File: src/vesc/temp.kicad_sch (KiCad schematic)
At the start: 3 parts

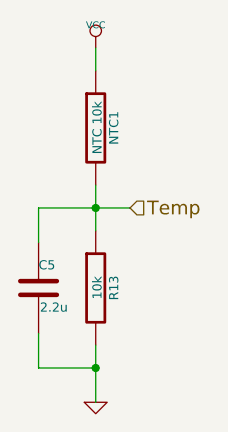
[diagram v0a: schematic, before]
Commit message: Fix component values
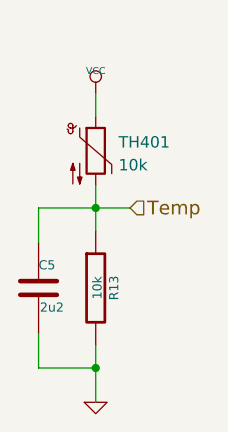
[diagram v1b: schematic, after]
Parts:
- removed NTC1: NTC 10k, Resistor_SMD:R_0603_1608Metric, symbol BLDC_4-rescue:R-RESCUE-BLDC_4
- added TH401: 10k, symbol Device:Thermistor_NTC
- C5: value 2.2u -> 2u2; footprint Capacitor_SMD:C_0603_1608Metric -> (none)
- R13: footprint Resistor_SMD:R_0603_1608Metric -> (none)
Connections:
- net Temp: now also TH401.2
- net VCC: now also TH401.1
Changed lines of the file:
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@@
 	(wire
 		(pts
-			(xy 147.32 74.93) (xy 147.32 77.47)
+			(xy 147.32 80.01) (xy 147.32 82.55)
 		)
 		(stroke
@@
 	(symbol
 		(lib_id "BLDC_4-rescue:R-RESCUE-BLDC_4")
-		(at 147.32 83.82 0)
-		(unit 1)
-		(exclude_from_sim no)
-		(in_bom yes)
-		(on_board yes)
-		(dnp no)
-		(property "Reference" "NTC1"
-			(at 149.352 83.82 90)
-			(effects
-				(font
-					(size 1.016 1.016)
-				)
-			)
-		)
-		(property "Value" "NTC 10k"
-			(at 147.4978 83.7946 90)
-			(effects
-				(font
-					(size 1.016 1.016)
-				)
-			)
-		)
-		(property "Footprint" "Resistor_SMD:R_0603_1608Metric"
-			(at 145.542 83.82 90)
-			(effects
-				(font
-					(size 0.762 0.762)
-				)
-				(hide yes)
-			)
-		)
-		(property "Datasheet" ""
-			(at 147.32 83.82 0)
-			(effects
-				(font
-					(size 0.762 0.762)
-				)
-			)
-		)
-		(property "Description" ""
-			(at 147.32 83.82 0)
-			(effects
-				(font
-					(size 1.27 1.27)
-				)
-			)
-		)
-		(pin "1"
-		)
-		(pin "2"
-		)
-		(instances
-			(project "Cheap FOCer 2 60mm"
-				(path "/8b53313b-c20e-4d2c-aeda-56c30dbca1c0/00000000-0000-0000-0000-000053ffb3e2"
-					(reference "NTC1")
-					(unit 1)
-				)
-			)
-		)
-	)
-	(symbol
-		(lib_id "BLDC_4-rescue:R-RESCUE-BLDC_4")
 		(at 147.32 101.6 0)
 		(unit 1)
@@
 			)
 		)
-		(property "Footprint" "Resistor_SMD:R_0603_1608Metric"
+		(property "Footprint" ""
 			(at 145.542 101.6 90)
 			(effects
@@
 			)
 		)
-		(property "Value" "2.2u"
+		(property "Value" "2u2"
 			(at 141.1224 103.759 0)
 			(effects
@@
 			)
 		)
-		(property "Footprint" "Capacitor_SMD:C_0603_1608Metric"
+		(property "Footprint" ""
 			(at 141.9352 105.41 0)
 			(effects
@@
 	(symbol
 		(lib_id "BLDC_4-rescue:VCC")
-		(at 147.32 74.93 0)
+		(at 147.32 80.01 0)
 		(unit 1)
 		(exclude_from_sim no)
@@
 		(dnp no)
 		(property "Reference" "#PWR021"
-			(at 147.32 72.39 0)
+			(at 147.32 77.47 0)
 			(effects
 				(font
@@
 		)
 		(property "Value" "VCC"
-			(at 147.32 72.39 0)
-			(effects
-				(font
-					(size 0.762 0.762)
-				)
-			)
-		)
-		(property "Footprint" ""
-			(at 147.32 74.93 0)
+			(at 147.32 77.47 0)
+			(effects
+				(font
+					(size 0.762 0.762)
+				)
+			)
+		)
+		(property "Footprint" ""
+			(at 147.32 80.01 0)
 			(effects
 				(font
@@
 		)
 		(property "Datasheet" ""
-			(at 147.32 74.93 0)
+			(at 147.32 80.01 0)
 			(effects
 				(font
@@
 		)
 		(property "Description" ""
-			(at 147.32 74.93 0)
+			(at 147.32 80.01 0)
 			(effects
 				(font
@@
 					(unit 1)
 				)
+			)
+		)
+	)
+	(symbol
+		(lib_id "Device:Thermistor_NTC")
+		(at 147.32 86.36 0)
+		(unit 1)
+		(exclude_from_sim no)
+		(in_bom yes)
+		(on_board yes)
+		(dnp no)
+		(fields_autoplaced yes)
+		(property "Reference" "TH401"
+			(at 149.86 85.4074 0)
+			(effects
+				(font
+					(size 1.27 1.27)
+				)
+				(justify left)
+			)
+		)
+		(property "Value" "10k"
+			(at 149.86 87.9474 0)
+			(effects
+				(font
+					(size 1.27 1.27)
+				)
+				(justify left)
+			)
+		)
+		(property "Footprint" ""
+			(at 147.32 85.09 0)
+			(effects
+				(font
+					(size 1.27 1.27)
+				)
+				(hide yes)
+			)
+		)
+		(property "Datasheet" "~"
+			(at 147.32 85.09 0)
+			(effects
+				(font
+					(size 1.27 1.27)
+				)
+				(hide yes)
+			)
+		)
+		(property "Description" "Temperature dependent resistor, negative temperature coefficient"
+			(at 147.32 86.36 0)
+			(effects
+				(font
+					(size 1.27 1.27)
+				)
+				(hide yes)
+			)
+		)
+		(pin "2"
+		)
+		(pin "1"
+		)
+		(instances
+			(project ""
+				(path "/8b53313b-c20e-4d2c-aeda-56c30dbca1c0/00000000-0000-0000-0000-000053ffb3e2"
+					(reference "TH401")
+					(unit 1)
+				)

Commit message: footprints - most resistors and caps, some ICs
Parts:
- C5: footprint (none) -> Capacitor_SMD:C_0201_0603Metric
- R13, TH401: footprint (none) -> Resistor_SMD:R_0402_1005Metric
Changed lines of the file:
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@@
 			)
 		)
-		(property "Footprint" ""
+		(property "Footprint" "Resistor_SMD:R_0402_1005Metric"
 			(at 145.542 101.6 90)
 			(effects
@@
 			)
 		)
-		(property "Footprint" ""
+		(property "Footprint" "Capacitor_SMD:C_0201_0603Metric"
 			(at 141.9352 105.41 0)
 			(effects
@@
 			)
 		)
-		(property "Footprint" ""
+		(property "Footprint" "Resistor_SMD:R_0402_1005Metric"
 			(at 147.32 85.09 0)
 			(effects

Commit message: footprints for remaining caps, resistors, diodes, MOSFETs. and ICs
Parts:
- C5: footprint Capacitor_SMD:C_0201_0603Metric -> Capacitor_SMD:C_1206_3216Metric
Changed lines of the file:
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@@
 			)
 		)
-		(property "Footprint" "Capacitor_SMD:C_0201_0603Metric"
+		(property "Footprint" "Capacitor_SMD:C_1206_3216Metric"
 			(at 141.9352 105.41 0)
 			(effects

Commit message: Correct footprints
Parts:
- C5: footprint Capacitor_SMD:C_1206_3216Metric -> Capacitor_SMD:C_0603_1608Metric
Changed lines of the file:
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@@
 			)
 		)
-		(property "Footprint" "Capacitor_SMD:C_1206_3216Metric"
+		(property "Footprint" "Capacitor_SMD:C_0603_1608Metric"
 			(at 141.9352 105.41 0)
 			(effects
